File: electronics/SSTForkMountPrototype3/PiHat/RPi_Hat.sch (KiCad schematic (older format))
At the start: 9 parts, among them CON1 BARREL_JACK, J1 RJ12, J3 M1 Encoder, J4 MPWR, J5 M2 Encoder, U1 pololu_MC33926, U2 pololu_D24V22F5, U3 Teensy_3.1

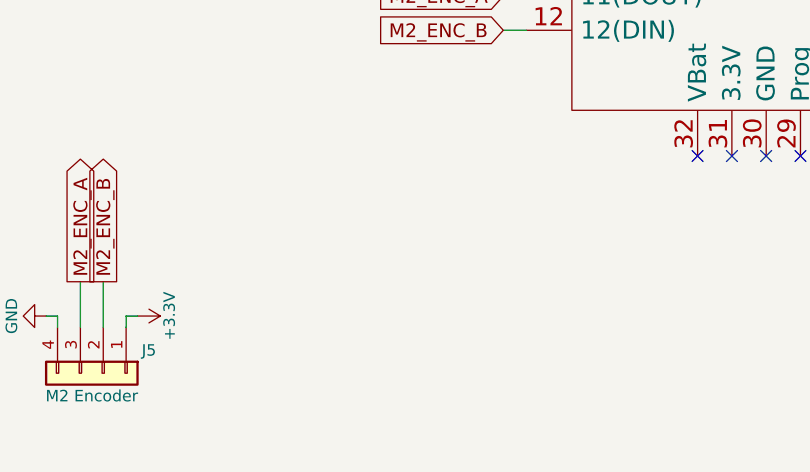
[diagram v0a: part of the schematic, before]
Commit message: RA DEC to M info
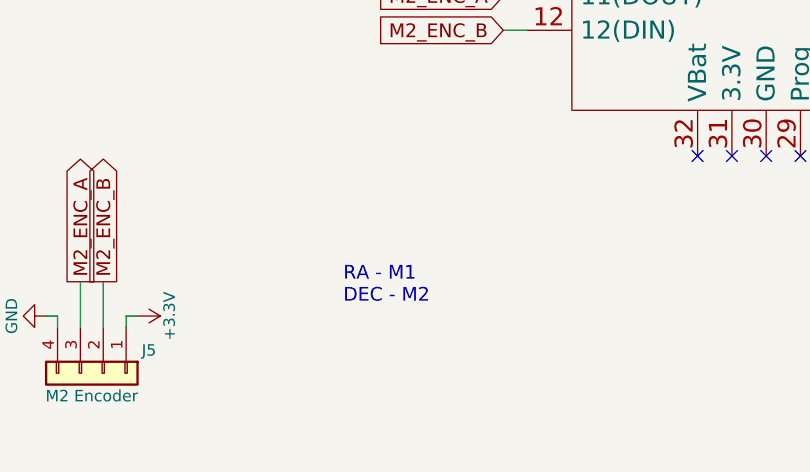
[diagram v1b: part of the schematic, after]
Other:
- note added: "RA - M1\nDEC - M2"
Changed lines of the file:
@@
 Wire Wire Line
 	7500 4850 7600 4850
+Text Notes 6800 6050 0    60   ~ 0
+RA - M1\nDEC - M2
 $EndSCHEMATC
